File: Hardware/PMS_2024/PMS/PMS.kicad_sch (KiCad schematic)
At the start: 101 parts, among them J1 RJ45_LED_Shielded, Q3 BSS138, Q4 IPB180N10S4-02, Q5 BSS138, Q5 SPD30P06PGBTMA1, Q7 BSS138, U1 Teensy4.1_DEV-16771, U10 ACS725xLCTR-20AB, U4 Opamp_Dual, U5 Opamp_Dual, U5 PKE3316ZPI, U6 Opamp_Dual, U7 ACS758xCB-200B-PFF, U9 OKI, U9 PKE3316ZPI

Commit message: Layout Started
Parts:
- removed C2: 10uF, Capacitor_THT:CP_Radial_D5.0mm_P2.00mm, symbol Device:C_Polarized_US
- removed C5: 10uF, Capacitor_SMD:C_0603_1608Metric_Pad1.08x0.95mm_HandSolder, symbol Device:C_Polarized_US
- removed Conn11: AndersonPP, MRDT_Connectors:Square_Anderson_2_H_Stacked, symbol MRDT_Connectors:AndersonPP
- removed D6: Green, LED_SMD:LED_0603_1608Metric_Pad1.05x0.95mm_HandSolder, symbol Device:LED
- removed Q4: IPB180N10S4-02, Package_TO_SOT_SMD:TO-263-6, symbol Transistor_FET:IPB180N10S4-02
- removed R27: 300, Resistor_SMD:R_0603_1608Metric_Pad0.98x0.95mm_HandSolder, symbol Device:R
- removed U9: OKI, MRDT_Devices:OKI_Horizontal, symbol MRDT_Devices:OKI
- added Conn18, Conn19, Conn20: Molex_SL_03, MRDT_Connectors:MOLEX_SL_03_Horizontal, symbol MRDT_Connectors:Molex_SL_03
- added D? (x2): Green, LED_SMD:LED_0603_1608Metric_Pad1.05x0.95mm_HandSolder, symbol Device:LED
- added Q5: SPD30P06PGBTMA1, Package_TO_SOT_SMD:TO-252-2, symbol Transistor_FET:QM6015D
- added R? (x2): 2k, Resistor_SMD:R_0603_1608Metric_Pad0.98x0.95mm_HandSolder, symbol Device:R
- added V1, V2, V3, V4: Via, MRDT_Drill_Holes:4_40_Hole, symbol MRDT_Drill_Holes:Via
- Conn17: renamed from Conn18; footprint (none) -> MRDT_Connectors:MOLEX_SL_07_Horizontal
- D?: renamed from D3; value Green -> Red
- R?: renamed from R48; value 300 -> 100
- renumbered BZ2 to BZ?, C6 to C1, C10 to C12, C11 to C13, C7 to C2, C1 to C3, C8 to C4, C12 to C5, C9 to C6, C13 to C7, C14 to C8, C15 to C9, C5 to C?, C2 to C?, Conn5 to Conn1, Conn6 to Conn10, Conn17 to Conn11, Conn16 to Conn12, Conn15 to Conn13, Conn13 to Conn15, Conn12 to Conn16, Conn4 to Conn2, Conn2 to Conn4, Conn1 to Conn5, Conn10 to Conn6, Conn9 to Conn7, Conn7 to Conn9, D8 to D3, D5 to D?, D7 to D?, Q3 to Q2, Q5 to Q3, Q7 to Q?, Q5 to Q?, Q4 to Q?, R4 to R17, R5 to R20, R9 to R21, R18 to R?, R23 to R?, R11 to R?, R26 to R?, R35 to R?, R14 to R?, R24 to R?, R28 to R?, R31 to R?, R39 to R?, R10 to R?, R36 to R?, R17 to R?, R38 to R?, R37 to R?, R41 to R?, R12 to R?, R30 to R?, R16 to R?, R19 to R?, R21 to R?, R34 to R?, R32 to R?, R29 to R?, R13 to R?, R40 to R?, R15 to R?, R20 to R?, R22 to R?, R42 to R?, U5 to U2, U9 to U3, U10 to U8, U6 to U?, U5 to U?, U4 to U?, U7 to U?, U9 to U?
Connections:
- net +5V is gone; now on net +3.3V: BZ?.1 (-), R?.2
- net RouterPi is gone; now on net Motor_PWR: Conn6.4 (PV+)
- net +3.3V: now also Conn18.1, Conn19.1, Conn20.1
- net Aux_PWR: now also Conn8.4 (PV+)
- net GND: now also R?.2, Conn18.2, Conn19.2, Conn20.2, D?.1 (K), D?.1 (K); no longer R?.1
- net LowCurrent_PWR: now also Conn11.4 (PV+), Conn12.4 (PV+), Q5.2 (D); no longer Conn7.4 (PV+), Conn8.4 (PV+)
- net Motor_PWR: now also Conn7.4 (PV+); no longer Conn10.4 (PV+), Conn9.4 (PV+)
- net NS_24V: now also Conn9.4 (PV+), R?.2; no longer Conn11.4 (PV+)
- net POE_24V: now also Conn10.4 (PV+), R?.2; no longer Conn12.4 (PV+)
- net PV: now also Q5.3 (S)
- net CS1: now reaches U1.27 (A13)
- net CS1: now also Conn20.3
- net CS2: now reaches U1.38 (A14)
- net CS2: now also Conn19.3
- net CS3: now reaches U1.39 (A15)
- net CS3: now also Conn18.3
- net at R?.1, R?.2: now also Q5.1 (G)
- net Buzzer-Teensy renamed Buzzer
- net Buzzer: now also R?.1; no longer R?.2
- new net: D?.2 (A), R?.1 (x2)
- no-connect marks 20 -> 38
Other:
- note added: "Battery Cells"
- note added: "Capacitor Bank"
- note added: "Current Sensing"
- note added: "Mounting VIAs"
- note added: "NS 24V"
- note added: "OKI 3.3V"
- note added: "POE 24V"
- note added: "SL Connectors"
- note added: "Status LEDs"
- note added: "Toggle Circuits"
- note removed: "+"
- note removed: "-"
- note removed: "Cell 1"
- note removed: "Cell 2"
- note removed: "Cell 3"
- note removed: "Cell 4"
- note removed: "Cell 5"
- note removed: "Cell 6"
- note removed: "LEDs"
- moved on the sheet: C1, C12, C13, C2, C3, C4, C5, C6, C7, C8, C9, C?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

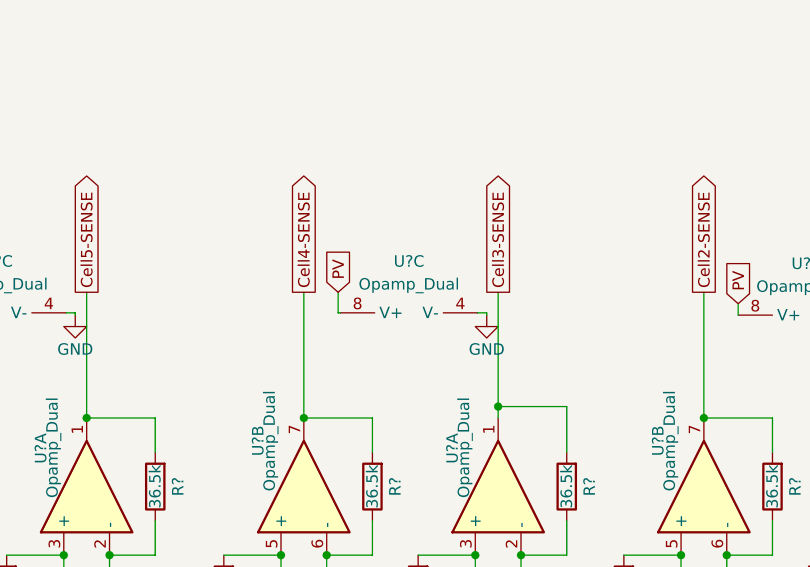
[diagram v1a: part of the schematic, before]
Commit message: Finished General Layout
All trace work still needs to be done
General layout is finished
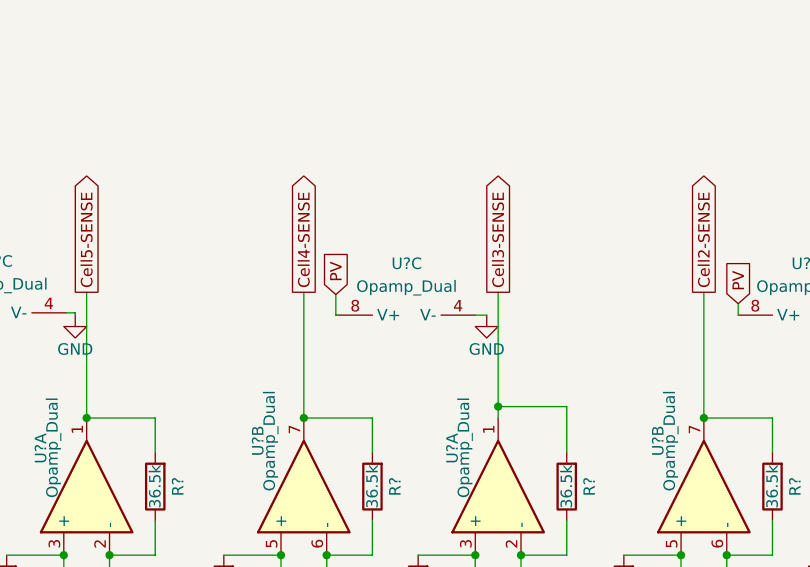
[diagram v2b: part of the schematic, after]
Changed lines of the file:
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@@
     (stroke (width 0) (type default))
   )
-  (wire (pts (xy 349.885 195.326) (xy 348.869 195.326))
-    (stroke (width 0) (type default))
-  )
   (wire (pts (xy 187.96 274.32) (xy 213.995 274.32))
     (stroke (width 0) (type default))
@@
     (stroke (width 0) (type default))
   )
+  (wire (pts (xy 348.615 195.58) (xy 349.885 195.58))
+    (stroke (width 0) (type default))
+  )
   (wire (pts (xy 156.845 46.355) (xy 156.845 45.085))
     (stroke (width 0) (type default))
@@
     (stroke (width 0) (type default))
   )
-  (wire (pts (xy 333.375 195.326) (xy 333.629 195.326))
+  (wire (pts (xy 333.121 195.58) (xy 333.375 195.58))
     (stroke (width 0) (type default))
   )
@@
     (stroke (width 0) (type default))
   )
-  (wire (pts (xy 349.885 195.58) (xy 349.885 195.326))
-    (stroke (width 0) (type default))
-  )
   (wire (pts (xy 303.53 97.155) (xy 299.085 97.155))
     (stroke (width 0) (type default))
@@
     (stroke (width 0) (type default))
   )
-  (wire (pts (xy 333.375 193.04) (xy 333.375 195.326))
+  (wire (pts (xy 333.121 193.294) (xy 333.121 195.58))
     (stroke (width 0) (type default))
   )
@@
     )
   )
-  (global_label "PV" (shape input) (at 333.375 193.04 90) (fields_autoplaced)
+  (global_label "PV" (shape input) (at 333.121 193.294 90) (fields_autoplaced)
     (effects (font (size 1.27 1.27)) (justify left))
-    (property "Intersheetrefs" "${INTERSHEET_REFS}" (at 333.375 187.6962 90)
+    (property "Intersheetrefs" "${INTERSHEET_REFS}" (at 333.121 187.9502 90)
       (effects (font (size 1.27 1.27)) (justify left) hide)
     )
@@
     )
   )
-  (symbol (lib_id "Device:Opamp_Dual") (at 341.249 192.786 90) (unit 3)
+  (symbol (lib_id "Device:Opamp_Dual") (at 340.995 193.04 90) (unit 3)
     (in_bom yes) (on_board yes) (dnp no) (fields_autoplaced)
-    (property "Reference" "U?" (at 341.249 189.611 90)
+    (property "Reference" "U?" (at 340.995 189.865 90)
       (effects (font (size 1.27 1.27)))
     )
-    (property "Value" "Opamp_Dual" (at 341.249 192.151 90)
+    (property "Value" "Opamp_Dual" (at 340.995 192.405 90)
       (effects (font (size 1.27 1.27)))
     )
-    (property "Footprint" "Package_SO:SO-8_3.9x4.9mm_P1.27mm" (at 341.249 192.786 0)
+    (property "Footprint" "Package_SO:SO-8_3.9x4.9mm_P1.27mm" (at 340.995 193.04 0)
       (effects (font (size 1.27 1.27)) hide)
     )
-    (property "Datasheet" "https://www.diodes.com/assets/Datasheets/AS358-358A-358B.pdf" (at 341.249 192.786 0)
+    (property "Datasheet" "https://www.diodes.com/assets/Datasheets/AS358-358A-358B.pdf" (at 340.995 193.04 0)
       (effects (font (size 1.27 1.27)) hide)
     )

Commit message: Changed Layout
Changed the entire layout
Most traces still need to be routed
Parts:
- removed R?: 1.0K, Resistor_SMD:R_0603_1608Metric_Pad0.98x0.95mm_HandSolder, symbol Device:R
- BZ?: footprint MRDT_Devices:BUZZER_SMI_1324_TW_5V_2_R -> Buzzer_Beeper:Buzzer_12x9.5RM7.6
- Conn16: footprint MRDT_Connectors:Square_Anderson_2_H_Stacked -> MRDT_Connectors:Square_Anderson_2_H_Side_By_Side_PV
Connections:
- net +3V3 is gone; now on net +3.3V: C13.1, U1.3.3V_1 (3.3V), U1.3.3V_2 (3.3V), U1.3.3V_3 (3.3V), U8.8 (VCC)
- net +BATT: now also U?.5 (IP-); no longer U?.4 (IP+)
- net PV: now also U?.4 (IP+); no longer U?.5 (IP-)

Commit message: Finished Layout + Traces
Finished Layout
Silkscreens still need to be added
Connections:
- net Aux_Enable: now also U1.31 (CTX3); no longer U1.1 (TX1)
- net Buzzer: now also U1.7 (RX2); no longer U1.8 (TX2)
- net CS1: now also U1.39 (A15); no longer U1.27 (A13)
- net CS2: now also U1.40 (A16); no longer U1.38 (A14)
- net CS3: now also U1.41 (A17); no longer U1.39 (A15)
- net CS_Aux: now also U1.27 (A13); no longer U1.16 (A2)
- net Cell3-SENSE: now also U1.16 (A2); no longer U1.14 (A0)
- net Cell4-SENSE: now also U1.17 (A3); no longer U1.15 (A1)
- net Cell5-SENSE: now also U1.14 (A0); no longer U1.40 (A16)
- net Cell6-SENSE: now also U1.15 (A1); no longer U1.41 (A17)
- net LowCurrent_Enable: now also U1.8 (TX2); no longer U1.7 (RX2)
- net Motor_Enable: now also U1.32 (OUT1B); no longer U1.0 (RX1)
- net NS_Enable: now also U1.1 (TX1); no longer U1.11 (MOSI)
- net POE_Enable: now also U1.0 (RX1); no longer U1.12 (MISO)

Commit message: Resistor Changes
Added a PV LED
Changed some resistor values
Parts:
- added D?: Green, LED_SMD:LED_0603_1608Metric_Pad1.05x0.95mm_HandSolder, symbol Device:LED
- added R?: 2k, Resistor_SMD:R_0603_1608Metric_Pad0.98x0.95mm_HandSolder, symbol Device:R
- R? (x3): value 3k -> 2k
- renumbered C3 to C1, C5 to C10, C7 to C11, C8 to C12, C9 to C13, C12 to C4, C13 to C5, C1 to C6, C2 to C7, C4 to C8, C6 to C9, Conn20 to Conn17, Conn19 to Conn18, Conn18 to Conn19, Conn17 to Conn20, D3 to D10, D2 to D9, Q2 to Q3, Q5 to Q4, Q3 to Q5, R17 to R3, R20 to R7, R21 to R8, U8 to U4, U2 to U5, U3 to U7
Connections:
- net GND: now also D?.1 (K)
- net PV: now also R?.2
- new net: D?.2 (A), R?.1
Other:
- moved on the sheet: D?, R?

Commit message: Footprint Change
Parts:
- removed C?: 10uF, Capacitor_SMD:C_0603_1608Metric_Pad1.08x0.95mm_HandSolder, symbol Device:C_Polarized_US
- removed C?: 10uF, Capacitor_THT:CP_Radial_D5.0mm_P2.00mm, symbol Device:C_Polarized_US
- added C2: 10uF, Capacitor_SMD:C_1206_3216Metric_Pad1.33x1.80mm_HandSolder, symbol Device:C
- added C3: 22uF, Capacitor_SMD:C_0603_1608Metric_Pad1.08x0.95mm_HandSolder, symbol Device:C
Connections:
- net +3.3V: now also C3.1
- net GND: now also C2.2, C3.2
- net PV: now also C2.1
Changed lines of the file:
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@@
     )
   )
+  (symbol (lib_id "Device:C") (at 184.785 41.275 0) (unit 1)
+    (in_bom yes) (on_board yes) (dnp no) (fields_autoplaced)
+    (property "Reference" "C3" (at 187.96 40.005 0)
+      (effects (font (size 1.27 1.27)) (justify left))
+    )
+    (property "Value" "22uF" (at 187.96 42.545 0)
+      (effects (font (size 1.27 1.27)) (justify left))
+    )
+    (property "Footprint" "Capacitor_SMD:C_0603_1608Metric_Pad1.08x0.95mm_HandSolder" (at 185.7502 45.085 0)
+      (effects (font (size 1.27 1.27)) hide)
+    )
+    (property "Datasheet" "~" (at 184.785 41.275 0)
+      (effects (font (size 1.27 1.27)) hide)
+    )
+    (pin "1")
+    (pin "2")
+    (instances
+      (project "PMS"
+        (path "/7091d3f0-e9de-4bc6-9639-20c8b3655d28"
+          (reference "C3") (unit 1)
+        )
+      )
+      (project "PowerBoard_2024"
+        (path "/8ad22d76-a558-4ba1-aeeb-dc7eabdc9e9b"
+          (reference "C?") (unit 1)
+        )
+      )
+    )
+  )
   (symbol (lib_id "Device:R") (at 229.235 116.84 270) (mirror x) (unit 1)
     (in_bom yes) (on_board yes) (dnp no)
@@
     )
   )
-  (symbol (lib_id "Device:C_Polarized_US") (at 184.785 41.275 0) (unit 1)
-    (in_bom yes) (on_board yes) (dnp no)
-    (property "Reference" "C?" (at 188.595 39.3699 0)
-      (effects (font (size 1.27 1.27)) (justify left))
-    )
-    (property "Value" "10uF" (at 187.325 41.275 0)
-      (effects (font (size 1.27 1.27)) (justify left))
-    )
-    (property "Footprint" "Capacitor_SMD:C_0603_1608Metric_Pad1.08x0.95mm_HandSolder" (at 184.785 41.275 0)
-      (effects (font (size 1.27 1.27)) hide)
-    )
-    (property "Datasheet" "~" (at 184.785 41.275 0)
-      (effects (font (size 1.27 1.27)) hide)
-    )
-    (pin "1")
-    (pin "2")
-    (instances
-      (project "2024Rev1"
-        (path "/62a5013b-27bd-4648-9844-b43a50a9ebdc"
-          (reference "C?") (unit 1)
-        )
-      )
-      (project "PMS"
-        (path "/7091d3f0-e9de-4bc6-9639-20c8b3655d28"
-          (reference "C3") (unit 1)
-        )
-      )
-    )
-  )
   (symbol (lib_id "Device:LED") (at 238.125 108.585 180) (unit 1)
     (in_bom yes) (on_board yes) (dnp no)
@@
     )
   )
-  (symbol (lib_id "Device:C_Polarized_US") (at 156.845 41.275 0) (unit 1)
-    (in_bom yes) (on_board yes) (dnp no) (fields_autoplaced)
-    (property "Reference" "C?" (at 160.655 39.37 0)
-      (effects (font (size 1.27 1.27)) (justify left))
-    )
-    (property "Value" "10uF" (at 160.655 41.91 0)
-      (effects (font (size 1.27 1.27)) (justify left))
-    )
-    (property "Footprint" "Capacitor_THT:CP_Radial_D5.0mm_P2.00mm" (at 156.845 41.275 0)
-      (effects (font (size 1.27 1.27)) hide)
-    )
-    (property "Datasheet" "~" (at 156.845 41.275 0)
-      (effects (font (size 1.27 1.27)) hide)
-    )
-    (pin "1")
-    (pin "2")
-    (instances
-      (project "2024Rev1"
-        (path "/62a5013b-27bd-4648-9844-b43a50a9ebdc"
-          (reference "C?") (unit 1)
-        )
-      )
-      (project "PMS"
-        (path "/7091d3f0-e9de-4bc6-9639-20c8b3655d28"
-          (reference "C2") (unit 1)
-        )
-      )
-    )
-  )
   (symbol (lib_id "Device:R") (at 313.055 214.63 180) (unit 1)
     (in_bom yes) (on_board yes) (dnp no)
@@
         )
       )
+    )
+  )
+  (symbol (lib_id "Device:C") (at 156.845 41.275 0) (unit 1)
+    (in_bom yes) (on_board yes) (dnp no) (fields_autoplaced)
+    (property "Reference" "C2" (at 159.766 40.0629 0)
+      (effects (font (size 1.27 1.27)) (justify left))
+    )
+    (property "Value" "10uF" (at 159.766 42.4871 0)
+      (effects (font (size 1.27 1.27)) (justify left))
+    )
+    (property "Footprint" "Capacitor_SMD:C_1206_3216Metric_Pad1.33x1.80mm_HandSolder" (at 157.8102 45.085 0)
+      (effects (font (size 1.27 1.27)) hide)
+    )
+    (property "Datasheet" "~" (at 156.845 41.275 0)
+      (effects (font (size 1.27 1.27)) hide)
+    )
+    (pin "1")
+    (pin "2")
+    (instances
+      (project "PMS"
+        (path "/7091d3f0-e9de-4bc6-9639-20c8b3655d28"
+          (reference "C2") (unit 1)
+        )
+      )
+      (project "PowerBoard_2024"
+        (path "/8ad22d76-a558-4ba1-aeeb-dc7eabdc9e9b"
+          (reference "C?") (unit 1)
+        )
+      )
